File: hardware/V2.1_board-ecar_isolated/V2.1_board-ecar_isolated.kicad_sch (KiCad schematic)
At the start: 116 parts, among them IC1 ATMEGA8A-P, J1 2x BATT IN, J10 24V, J11 18V, J12 5V, J13 ADC reserve [5V, in, GND], J14 IGBT [Gate, GND], J16 UART [GND, RX, TX], J17 2x Switch (to 5V) [PC3, PC2], J18 Relay contacts [NO, COM, NC]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

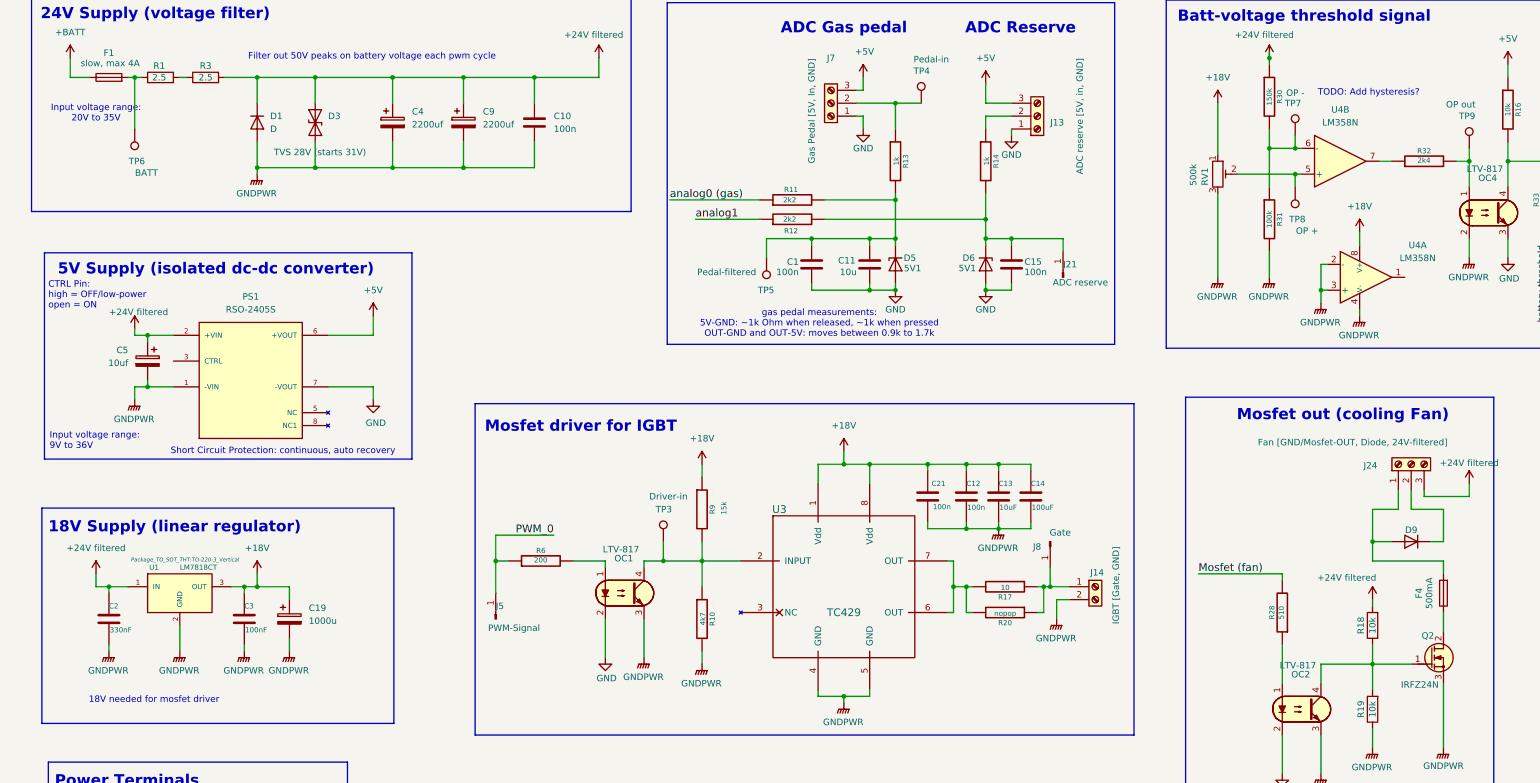
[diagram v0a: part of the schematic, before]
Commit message: pcb: Update schematic (mosfet name, actual R value)
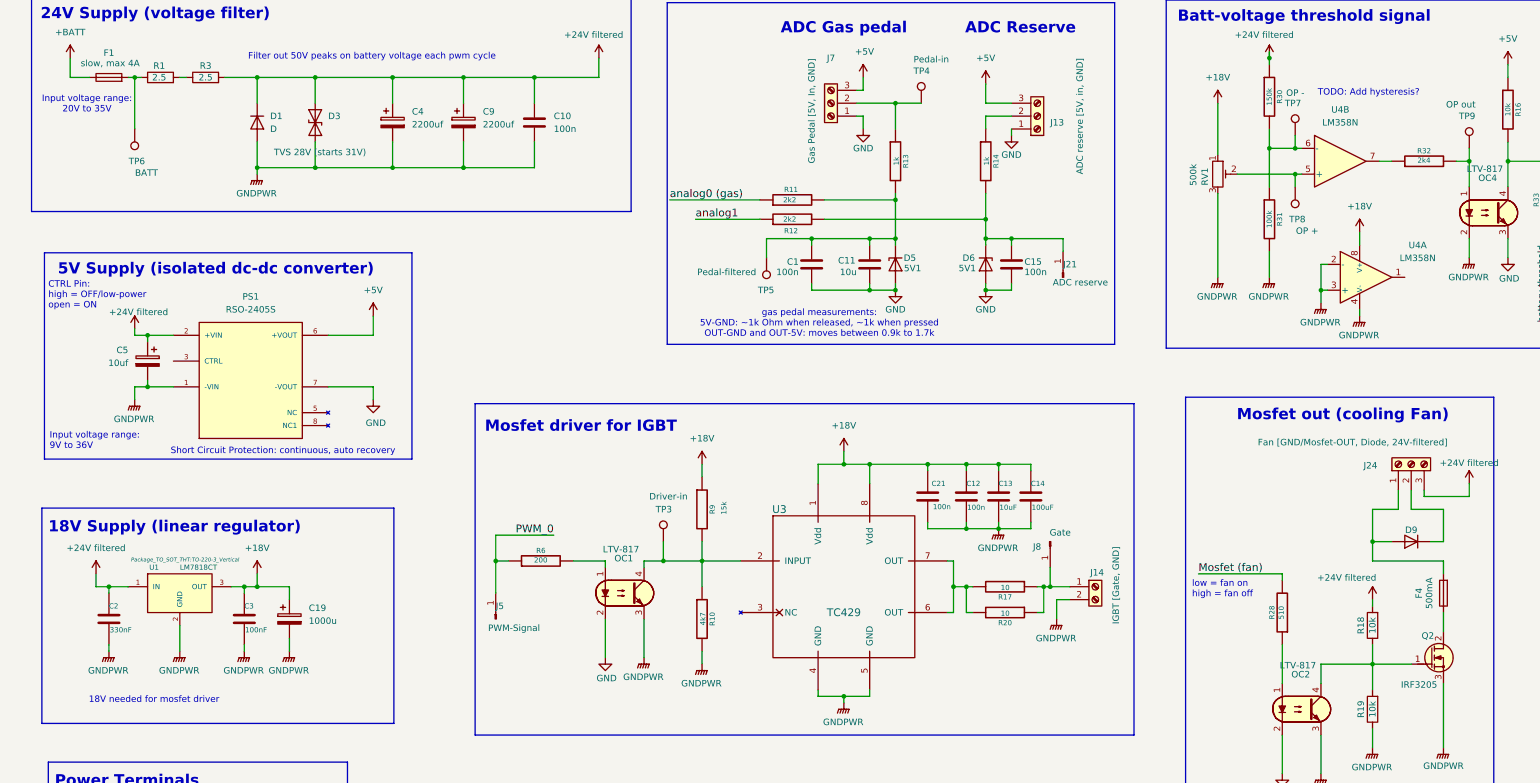
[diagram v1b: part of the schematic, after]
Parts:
- Q2: value IRFZ24N -> IRF3205
- R20: value nopop -> 10
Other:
- note added: "low = fan on high = fan off"
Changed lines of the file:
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@@
 	(text "Input voltage range: \n20V to 35V"
 		(exclude_from_sim no)
-		(at 27.94 38.862 0)
+		(at 26.162 37.084 0)
 		(effects
 			(font
@@
 		)
 	)
+	(text "low = fan on\nhigh = fan off"
+		(exclude_from_sim no)
+		(at 243.84 132.588 0)
+		(effects
+			(font
+				(size 1.27 1.27)
+			)
+			(justify left)
+		)
+	)
 	(text "2x Digital input\n(Switches to 5V)"
 		(exclude_from_sim no)
@@
 			)
 		)
-		(property "Value" "IRFZ24N"
+		(property "Value" "IRF3205"
 			(at 284.988 151.384 0)
 			(effects
@@
 			)
 		)
-		(property "Value" "nopop"
+		(property "Value" "10"
 			(at 207.0354 137.3378 90)
 			(effects
